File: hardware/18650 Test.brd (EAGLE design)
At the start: 68.6 x 22.9 mm, 3 parts

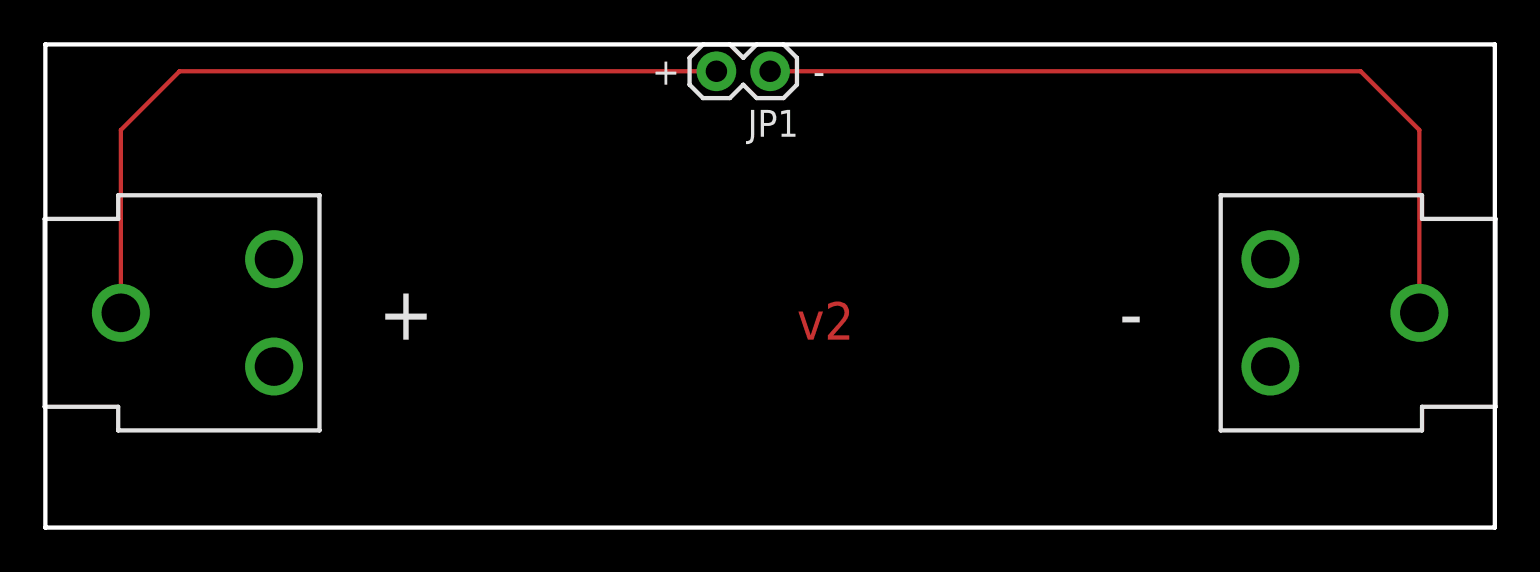
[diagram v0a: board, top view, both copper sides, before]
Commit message: v2 with Charge/Discharge MOSFET control and cell balancing
Many changes. Added large MOSFETs and pack interface circuitry. Added
small MOSFETs for individual cell balancing/charging. Corrected
Thermistor pull down error. All FPs pass 1:1 check.
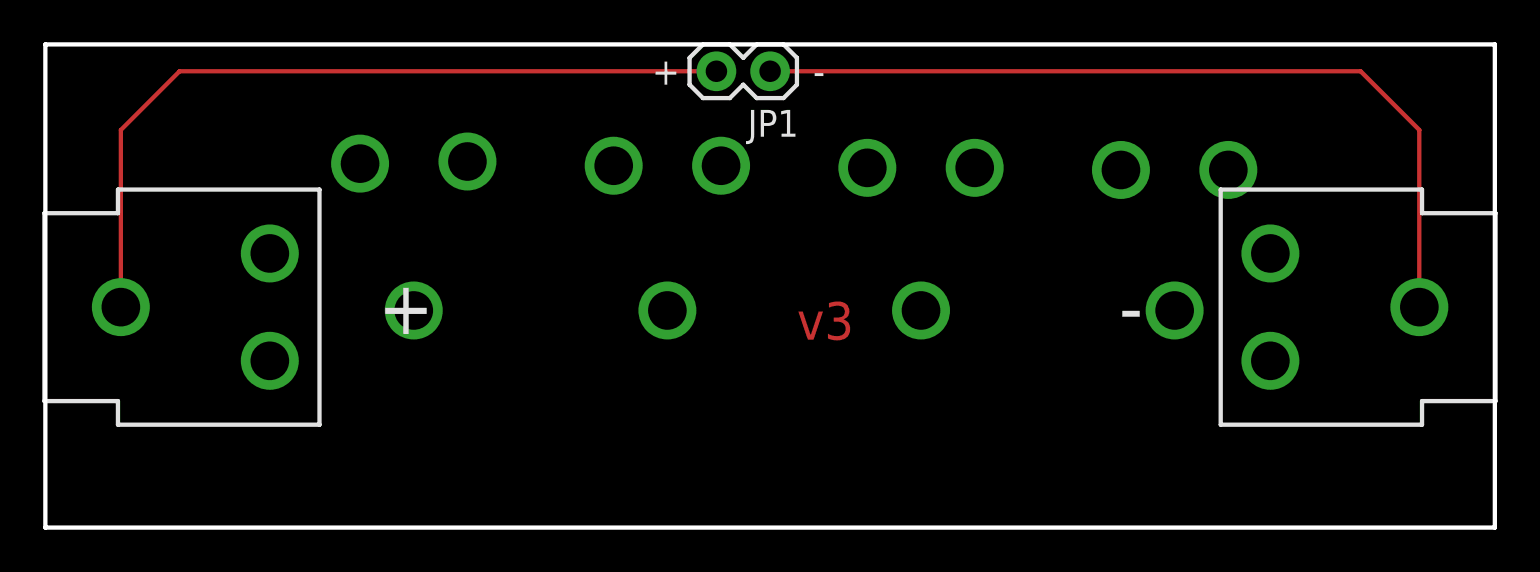
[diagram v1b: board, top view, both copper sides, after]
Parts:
- added B3: BATTERY, bq769x0:18650-TEST
- moved B1 0.27 mm to (34.3, 10.4)
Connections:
- new net +: B3.PWR@4
- new net -: B3.PWR@3
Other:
- board text added: "v3"
- board text removed: "v2"
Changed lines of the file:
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@@
 <text x="28.702" y="20.955" size="1.27" layer="21" font="vector" ratio="15">+</text>
 <text x="36.322" y="20.955" size="1.27" layer="21" font="vector" ratio="15">-</text>
-<text x="35.56" y="8.89" size="1.778" layer="1" font="vector" ratio="15">v2</text>
+<text x="35.56" y="8.89" size="1.778" layer="1" font="vector" ratio="15">v3</text>
 </plain>
 <attributes>
@@
 <elements>
 <element name="FRAME1" library="SparkFun-Aesthetics" package="CREATIVE_COMMONS" value="FRAME-LETTER" x="-0.65105625" y="-21.59"/>
-<element name="B1" library="bq769x0" package="18650-HOLDER" value="BATTERY18650" x="34.29" y="10.16"/>
+<element name="B1" library="bq769x0" package="18650-HOLDER" value="BATTERY18650" x="34.29" y="10.43"/>
 <element name="JP1" library="SparkFun-Connectors" package="1X02" value="M02PTH" x="34.29" y="21.59" rot="R180"/>
+<element name="B3" library="bq769x0" package="18650-TEST" value="BATTERY" x="11.43" y="20.32" rot="MR90"/>
 </elements>
 <signals>
@@
 <contactref element="B1" pad="PWR@1"/>
 <contactref element="JP1" pad="2"/>
-<wire x1="3.572" y1="10.16" x2="3.572" y2="18.812" width="0.2032" layer="1"/>
+<wire x1="3.572" y1="10.43" x2="3.572" y2="18.812" width="0.2032" layer="1"/>
 <wire x1="3.572" y1="18.812" x2="6.35" y2="21.59" width="0.2032" layer="1"/>
 <wire x1="6.35" y1="21.59" x2="31.75" y2="21.59" width="0.2032" layer="1"/>
@@
 <contactref element="B1" pad="GND@1"/>
 <contactref element="JP1" pad="1"/>
-<wire x1="65.008" y1="10.16" x2="65.008" y2="18.812" width="0.2032" layer="1"/>
+<wire x1="65.008" y1="10.43" x2="65.008" y2="18.812" width="0.2032" layer="1"/>
 <wire x1="65.008" y1="18.812" x2="62.23" y2="21.59" width="0.2032" layer="1"/>
 <wire x1="62.23" y1="21.59" x2="34.29" y2="21.59" width="0.2032" layer="1"/>
@@
 </polygon>
 </signal>
+<signal name="-">
+<contactref element="B3" pad="PWR@3"/>
+</signal>
+<signal name="+">
+<contactref element="B3" pad="PWR@4"/>
+</signal>
 </signals>
